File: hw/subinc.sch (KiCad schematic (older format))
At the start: 25 parts

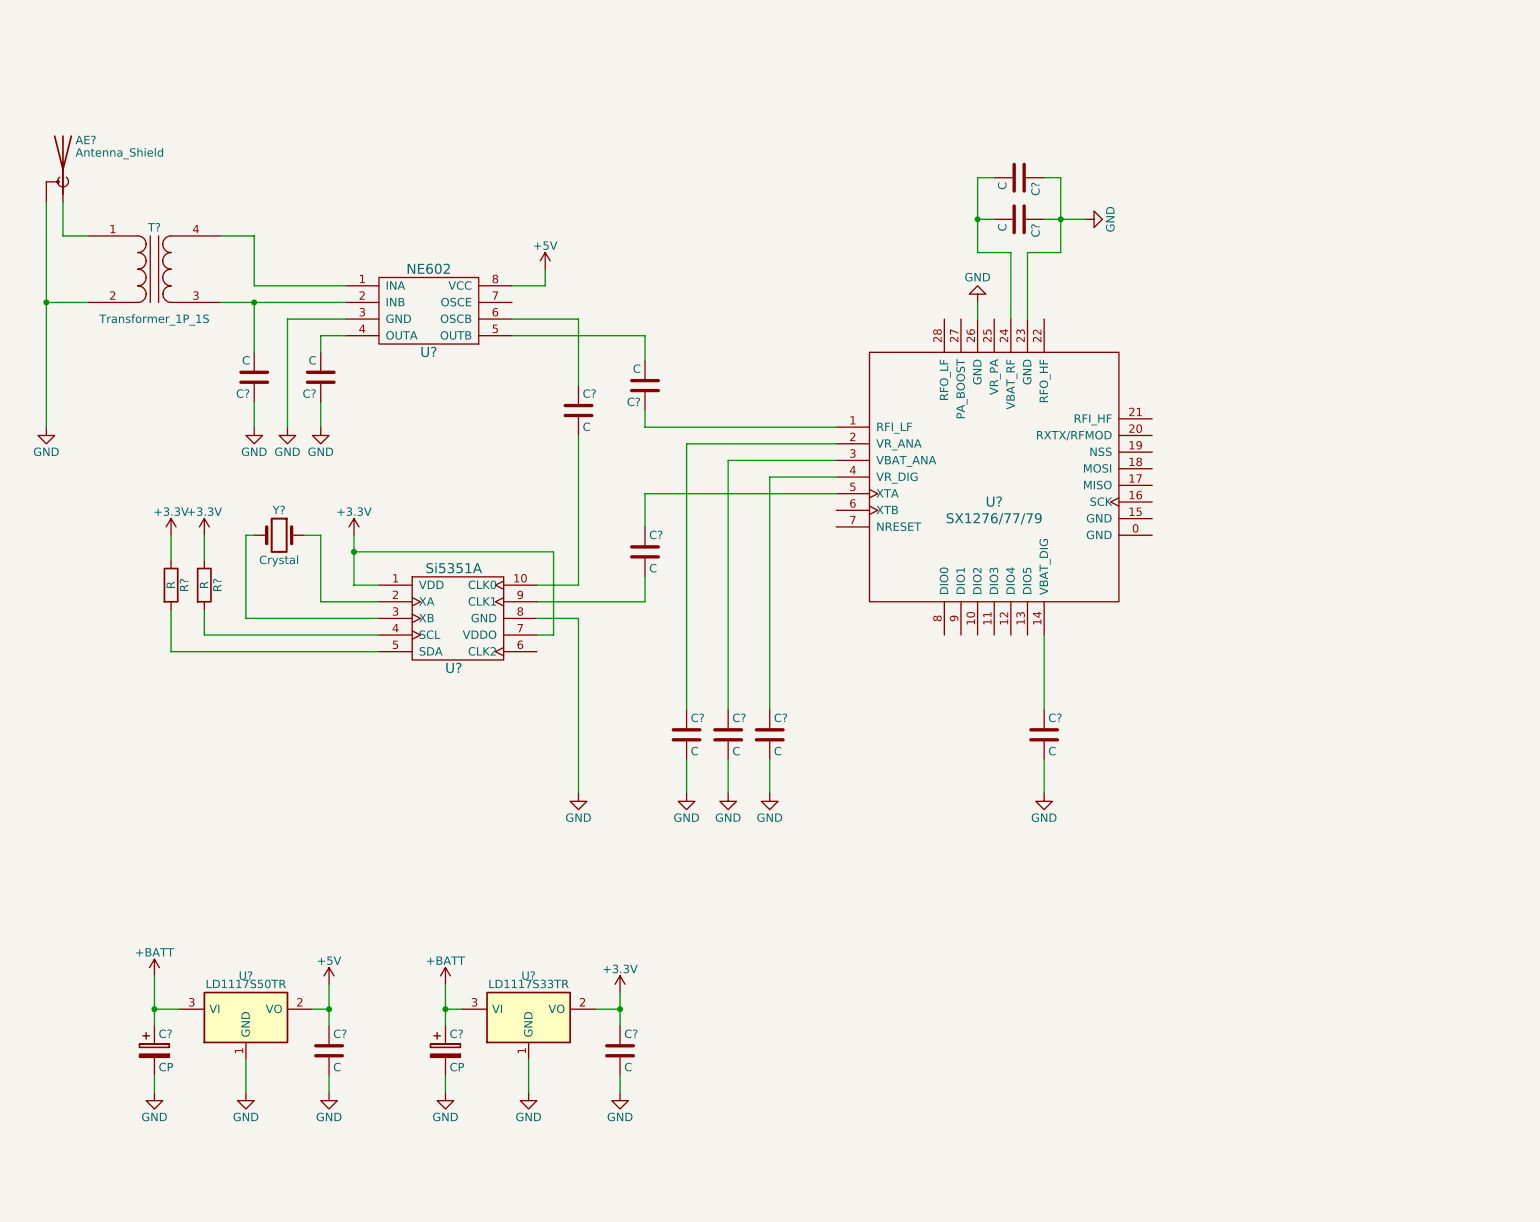
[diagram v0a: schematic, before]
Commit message: Adding multiband receiver schematic
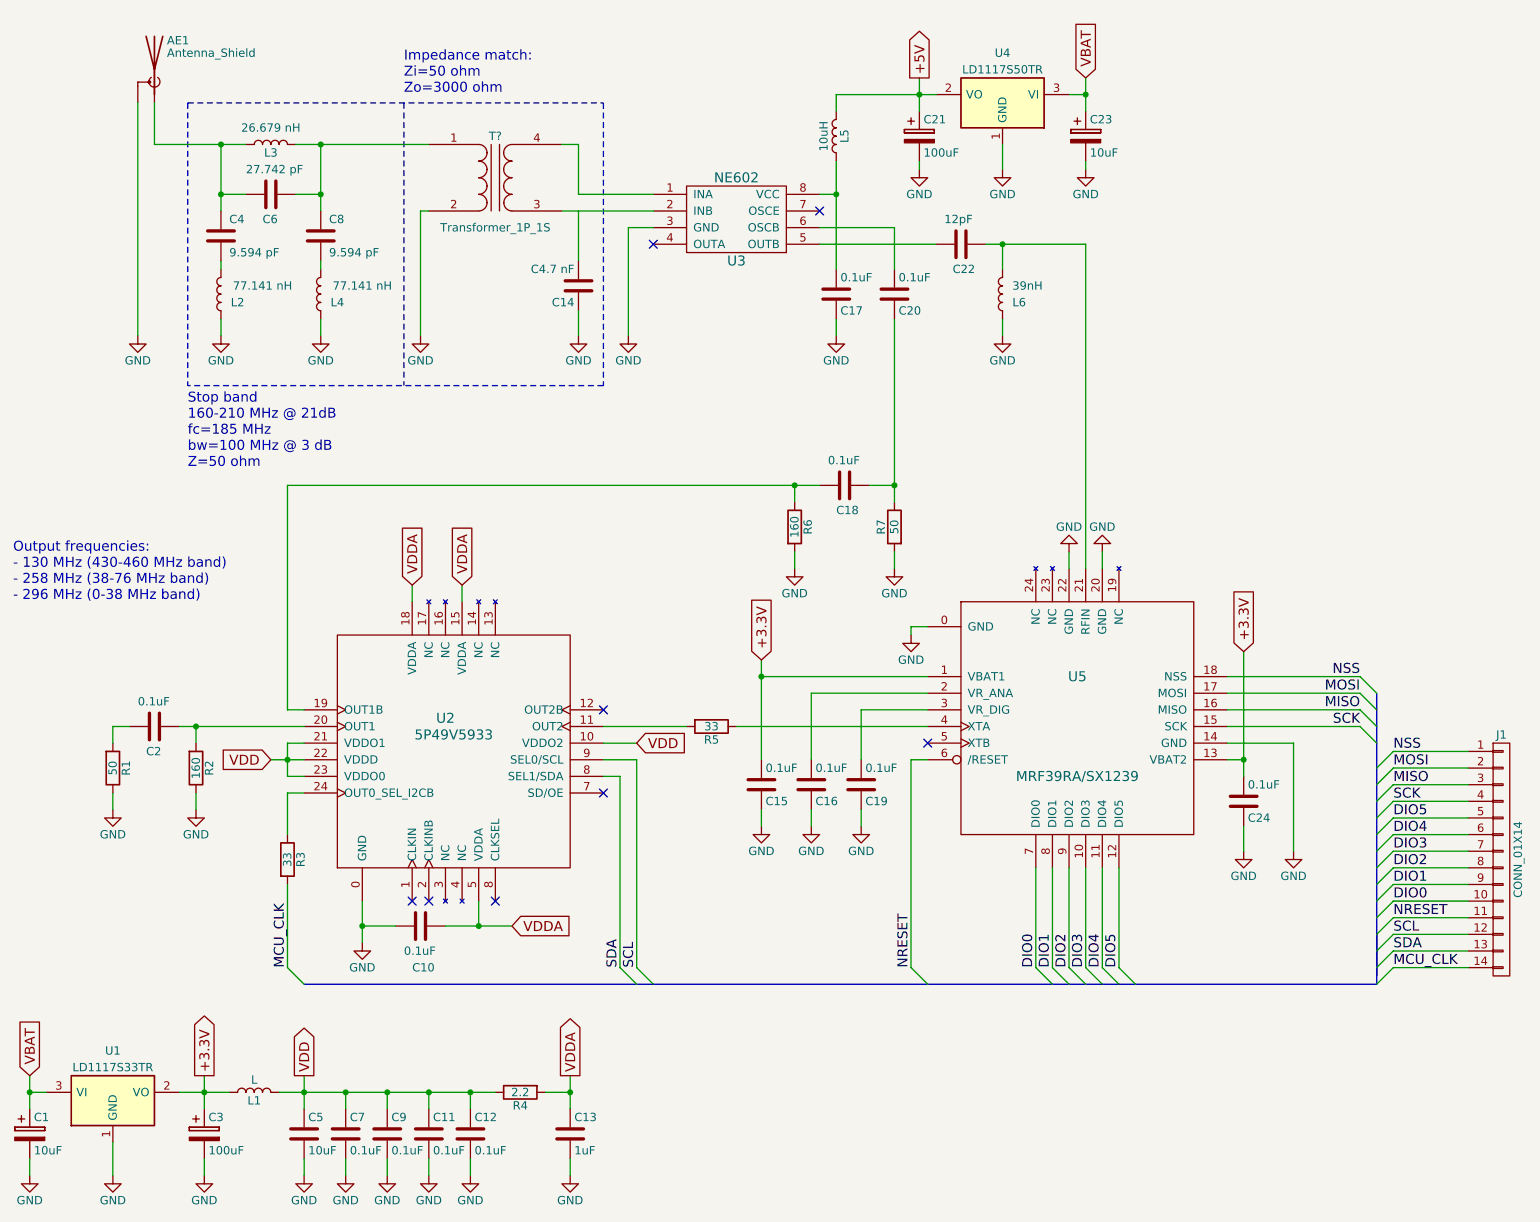
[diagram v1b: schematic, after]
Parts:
- removed C? (x10): C, symbol C
- removed C? (x2): CP, symbol CP
- removed T?: Transformer_1P_1S, symbol Transformer_1P_1S
- removed U?: Si5351A, symbol Si5351A
- removed U?: SX1276/77/79, symbol SX1276/77/79
- removed Y?: Crystal, symbol Crystal
- added C1, C23: 10uF, symbol CP
- added C10, C11, C12, C15, C16, C17, C19, C2, C20, C24, C7, C9: 0.1uF, symbol C
- added C13: 1uF, symbol C
- added C21, C3: 100uF, symbol CP
- added C4, C8: 9.594 pF, symbol C
- added C5: 10uF, symbol C
- added C6: 27.742 pF, symbol C
- added J1: CONN_01X14, symbol CONN_01X14
- added L1: L, symbol L
- added L2, L4: 77.141 nH, symbol L
- added L3: 26.679 nH, symbol L
- added L5: 10uH, symbol L
- added L6: 39nH, symbol L
- added R1, R7: 50, symbol R
- added R2: 160, symbol R
- added R4: 2.2, symbol R
- added R5: 33, symbol R
- added T?: Transformer_1P_1S, symbol Transformer_1P_1S
- added U2: 5P49V5933, symbol 5P49V5933
- added U5: MRF39RA/SX1239, symbol MRF39RA/SX1239
- C14: renamed from C?; value C -> C4.7 nF
- C18: renamed from C?; value C -> 0.1uF
- C22: renamed from C?; value C -> 12pF
- R3: renamed from R?; value R -> 33
- R6: renamed from R?; value R -> 160
- gave numbers to parts that had none: 4
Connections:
- net +5V: now also C21.1, L5.2; no longer U3.8 (VCC)
- net GND: now also R6.2, C1.2, C10.2, C11.2, C12.2, C13.2, C15.1, C16.1, C17.1, C19.1, C21.2, C23.2, C24.1, C3.2, C5.2, C7.2, C9.2, L2.1, L4.1, L6.1, R1.1, R2.1, R7.2, T?.2 (AB), U2.0 (GND), U5.0 (GND), U5.14 (GND), U5.20 (GND), U5.22 (GND)
- net at C18.2: now also R6.1, U2.19 (OUT1B)
- net MCU_CLK: now reaches R3.2
- net MCU_CLK: now also J1.14 (P14)
- net at C22.1: now also L6.2, U5.21 (RFIN)
- net at U3.1 (INA): now also T?.4 (SB)
- net at U3.2 (INB): now also T?.3 (SA); no longer C14.2
- net at U3.6 (OSCB): now also C20.2; no longer C18.1
- net at AE1.1 (A): now also C4.2, C6.2, L3.1
- removed net +3V3: R3.1, R6.1, U1.2 (VO)
- net +BATT renamed VBAT
- net VBAT: now also C1.1, C23.1
- new net: C17.2, L5.1, U3.8 (VCC)
- new net: R3.1, U2.24 (OUT0_SEL_I2CB)
- new net: C18.1, C20.1, R7.1
- new net: C6.1, C8.2, L3.2, T?.1 (AA)
- new net: C8.1, L4.2
- new net: C4.1, L2.2
- new net: C16.2, U5.2 (VR_ANA)
- new net: C19.2, U5.3 (VR_DIG)
- new net: R5.1, U5.4 (XTA)
- new net: R5.2, U2.11 (OUT2)
- new net: C2.1, R2.2, U2.20 (OUT1)
- new net: C2.2, R1.2
- new net +3.3V: C15.2, C24.2, C3.1, L1.1, U1.2 (VO), U5.1 (VBAT1), U5.13 (VBAT2)
- new net DIO0: J1.10 (P10), U5.7 (DIO0)
- new net DIO1: J1.9 (P9), U5.8 (DIO1)
- new net DIO2: J1.8 (P8), U5.9 (DIO2)
- new net DIO3: J1.7 (P7), U5.10 (DIO3)
- new net DIO4: J1.6 (P6), U5.11 (DIO4)
- new net DIO5: J1.5 (P5), U5.12 (DIO5)
- new net MISO: J1.3 (P3), U5.16 (MISO)
- new net MOSI: J1.2 (P2), U5.17 (MOSI)
- new net NRESET: J1.11 (P11), U5.6 (/RESET)
- new net NSS: J1.1 (P1), U5.18 (NSS)
- new net SCK: J1.4 (P4), U5.15 (SCK)
- new net SCL: J1.12 (P12), U2.9 (SEL0/SCL)
- new net SDA: J1.13 (P13), U2.8 (SEL1/SDA)
- new net VDD: C11.1, C12.1, C5.1, C7.1, C9.1, L1.2, R4.1, U2.10 (VDDO2), U2.21 (VDDO1), U2.22 (VDDD), U2.23 (VDDO0)
- new net VDDA: C10.1, C13.1, R4.2, U2.15 (VDDA), U2.18 (VDDA), U2.5 (VDDA)
- no-connect marks 0 -> 8
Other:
- note added: "Impedance match:\nZi=50 ohm\nZo=3000 ohm"
- note added: "Output frequencies:\n- 130 MHz (430-460 MHz band)\n- 258 MHz (38-76 MHz band)\n- 296 MHz (0-38 MHz band)"
- note added: "Stop band\n160-210 MHz @ 21dB\nfc=185 MHz\nbw=100 MHz @ 3 dB\nZ=50 ohm"
- moved on the sheet: AE1, C14, C18, C22, R3, R6, U1, U3, U4

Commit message: Some little fixes
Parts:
- C6: renamed from C22; value 12pF -> 1pF
- L5: renamed from L6; value 39nH -> 297nH
- gave numbers to parts that had none: 1
- renumbered C21 to C1, C18 to C10, C2 to C11, C15 to C12, C16 to C13, C19 to C14, C24 to C15, C10 to C16, C1 to C17, C3 to C18, C5 to C19, C23 to C2, C7 to C20, C9 to C21, C11 to C22, C12 to C23, C13 to C24, C6 to C3, C8 to C5, C14 to C7, C17 to C8, C20 to C9, L5 to L1, L3 to L2, L2 to L3, L1 to L6, R6 to R1, R7 to R2, R5 to R3, R1 to R4, R2 to R5, R3 to R6, R4 to R7, U4 to U1, U3 to U2, U5 to U3, U2 to U4, U1 to U5
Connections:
- net at C6.2, U2.5 (OUTB): now also L5.2
- net at C6.1, U3.21 (RFIN): no longer L5.2
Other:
- note added: "Impedance match:\nZi=1500 ohm\nZo=200 ohm\nHigh pass 240 MHz"
- note added: "Impedance match:\nZi=50 ohm\nZo=3000 ohm\nLow pass 500 MHz"
- note removed: "Impedance match:\nZi=50 ohm\nZo=3000 ohm"
- moved on the sheet: C6, L5
